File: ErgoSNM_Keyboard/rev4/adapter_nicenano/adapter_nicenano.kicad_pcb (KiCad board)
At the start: 2 copper layers, 30.5 x 34.9 mm, 8 parts, among them J1 Conn_01x13, J2 Conn_01x03, J3 Conn_01x13, J4 Conn_01x30

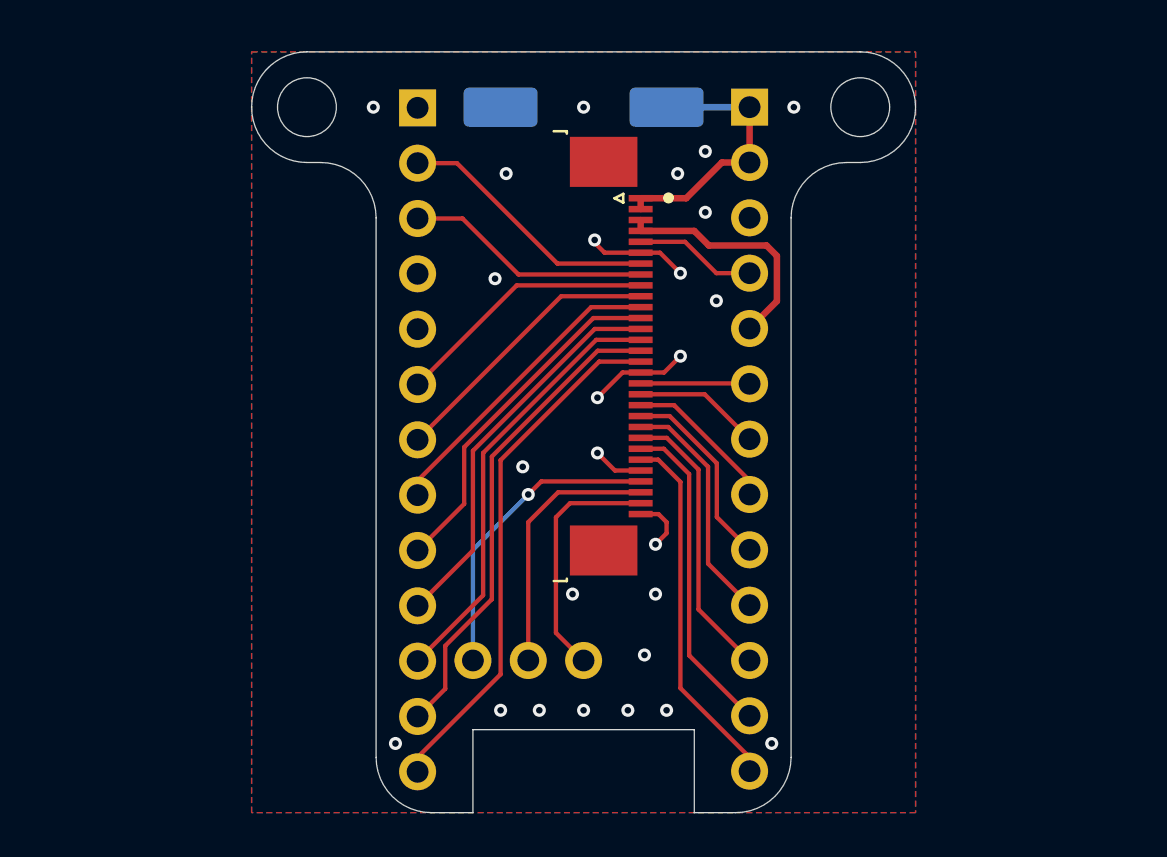
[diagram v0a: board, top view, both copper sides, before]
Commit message: feat: add v4 mdbt50q board
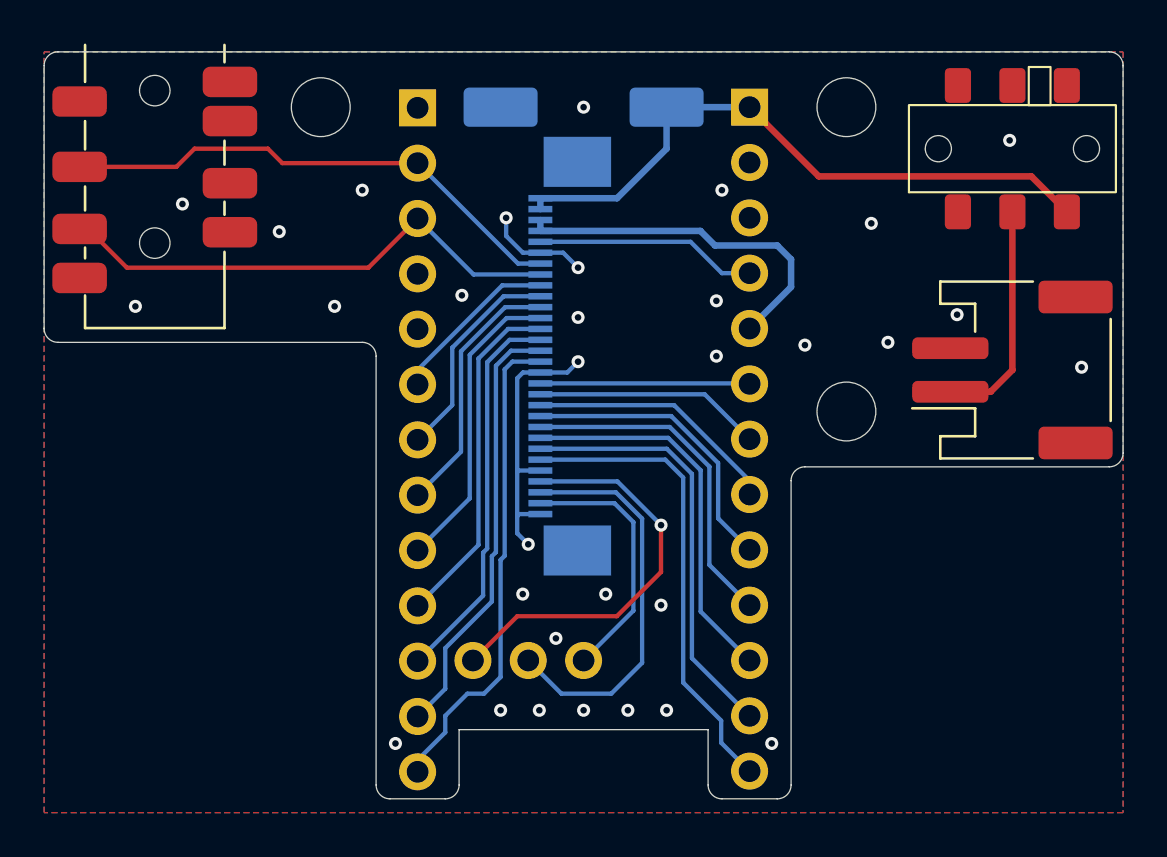
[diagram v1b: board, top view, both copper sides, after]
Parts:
- added H3: MountingHole, MountingHole:MountingHole_2.7mm_M2.5_ISO7380, F.Cu at (146.7, 105.4)
- added J5: Conn_Batt, Connector_JST:JST_PH_S2B-PH-SM4-TB_1x02-1MP_P2.00mm_Horizontal, F.Cu at (154.3, 103.5)
- added SW1: SW_DPDT_x2, ErgoSNM_Keyboard:MSKT-22D14-T, F.Cu at (154.3, 93.3)
- added TRRS1: PJ-393_TRRS_8P, ErgoSNM_Keyboard:PJ-393 8P TRRS, F.Cu at (114.9, 94.0)
- J4: moved to B.Cu
- moved J4 1.90 mm to (134.0, 102.9)
- moved H1 0.64 mm to (122.6, 91.4)
- moved H2 0.63 mm to (146.7, 91.4)
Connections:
- J3 pad 2: +BATT -> unconnected-(J3-Pin_2-Pad2)
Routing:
- net +BATT: track 12.5 -> 29.5 mm
- net P0.08: track 11.3 -> 23.9 mm
- net P0.06: track 12.1 -> 23.7 mm
- net Net-(J5-Pin_1): track 0.00 -> 10.5 mm
- net P1.02: track 12.1 -> 18.2 mm
- net +3.3V: track 11.1 -> 16.5 mm
- net P0.09: track 16.8 -> 21.6 mm
- net P1.01: track 14.1 -> 18.8 mm
- net P0.10: track 15.0 -> 19.6 mm
- net P1.13: track 11.0 -> 15.6 mm
- net P1.15: track 8.99 -> 13.6 mm
- net P1.11: track 13.0 -> 17.6 mm
- net RESET: track 5.60 -> 10.2 mm
- net P0.31: track 5.01 -> 9.61 mm
- net P0.29: track 5.85 -> 10.5 mm
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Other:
- board size 30.5 x 34.9 mm -> 49.5 x 34.3 mm
